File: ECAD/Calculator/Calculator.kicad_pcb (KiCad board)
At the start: 2 copper layers, 156 x 81.5 mm, 30 parts, among them SW1 Switch_Tactile_ESwitch, SW10 Switch_Tactile_ESwitch, SW11 Switch_Tactile_ESwitch, SW12 Switch_Tactile_ESwitch, SW13 Switch_Tactile_ESwitch, SW14 Switch_Tactile_ESwitch, SW15 Switch_Tactile_ESwitch, SW16 Switch_Tactile_ESwitch, SW17 Switch_Tactile_ESwitch, SW18 Switch_Tactile_ESwitch, SW19 Switch_Tactile_ESwitch, SW2 Switch_Tactile_ESwitch, SW20 Switch_Tactile_ESwitch, SW3 Switch_Tactile_ESwitch, SW4 Switch_Tactile_ESwitch, SW5 Switch_Tactile_ESwitch, SW6 Switch_Tactile_ESwitch, SW7 Switch_Tactile_ESwitch, SW8 Switch_Tactile_ESwitch, SW9 Switch_Tactile_ESwitch

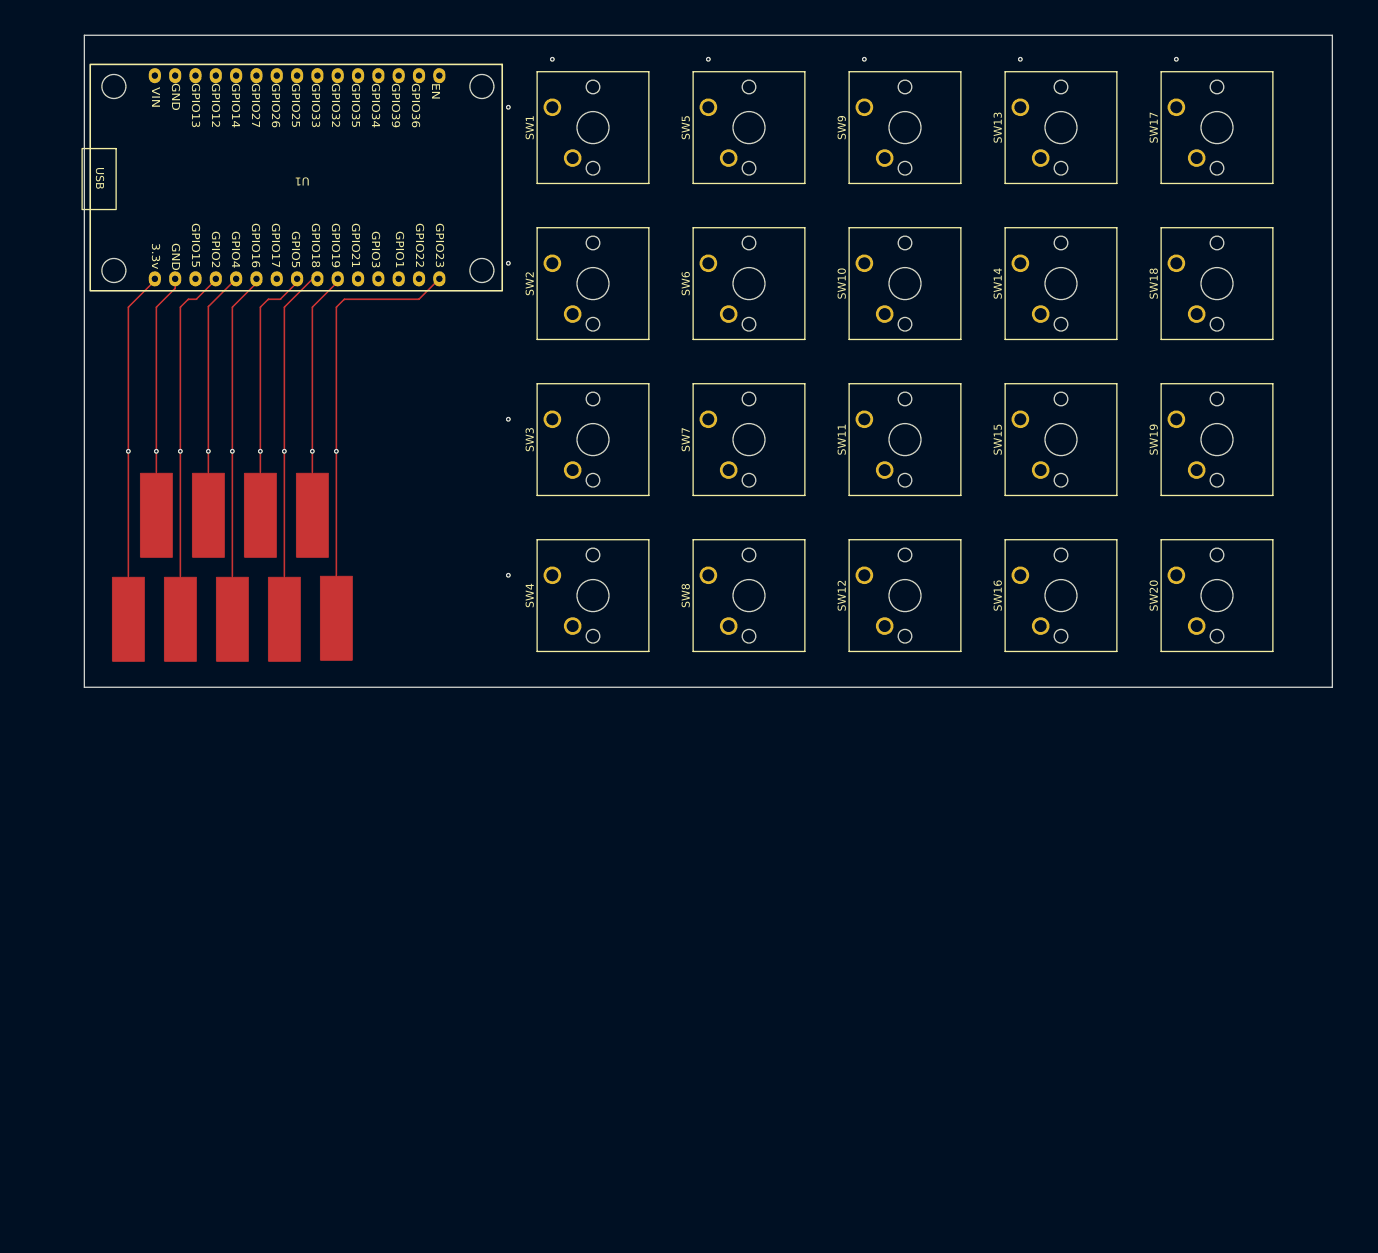
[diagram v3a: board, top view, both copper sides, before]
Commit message: Fixed switch placement
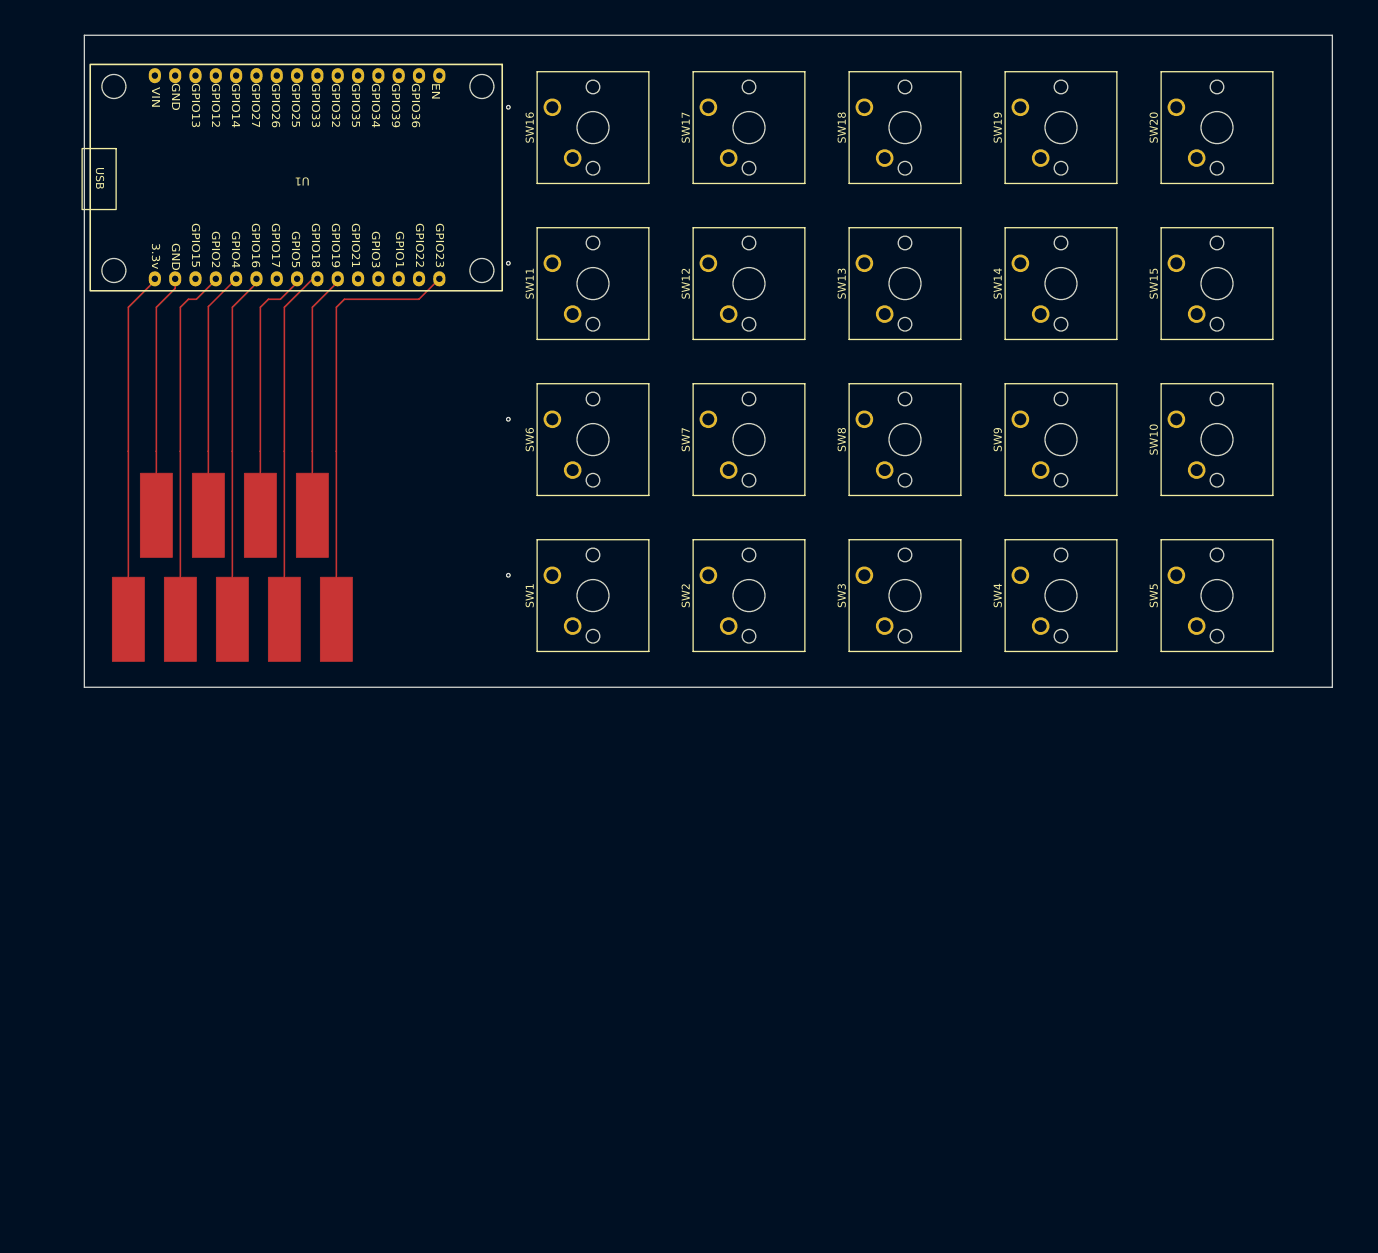
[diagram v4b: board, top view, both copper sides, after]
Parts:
- moved SW16 82.7 mm to (84.5, 27.0)
- moved SW5 82.7 mm to (162.5, 85.5)
- moved SW1 58.5 mm to (84.5, 85.5)
- moved SW17 58.5 mm to (104.0, 27.0)
- moved SW20 58.5 mm to (162.5, 27.0)
- moved SW4 58.5 mm to (143.0, 85.5)
- moved SW10 43.6 mm to (162.5, 66.0)
- moved SW11 43.6 mm to (84.5, 46.5)
- moved SW12 43.6 mm to (104.0, 46.5)
- moved SW18 43.6 mm to (123.5, 27.0)
- moved SW19 43.6 mm to (143.0, 27.0)
- moved SW2 43.6 mm to (104.0, 85.5)
- moved SW3 43.6 mm to (123.5, 85.5)
- moved SW9 43.6 mm to (143.0, 66.0)
- moved SW13 27.6 mm to (123.5, 46.5)
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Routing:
- net /VCC: vias 1 -> 0
- net /SDO(MISO): vias 1 -> 0
- net /SDI(MOSI): vias 1 -> 0
- net /SCK: vias 1 -> 0
- net /RESET: vias 1 -> 0
- net /LED: vias 1 -> 0
- net /GND: vias 1 -> 0
- net /DC/RS: vias 1 -> 0
- net /CS: vias 1 -> 0
- net (no net): vias 9 -> 4

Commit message: Refactor schematic: Remove unnecessary wires and update connections in Calculator.kicad_sch Added keyboard matrix wiring in PCB and mounting holes for enclosure
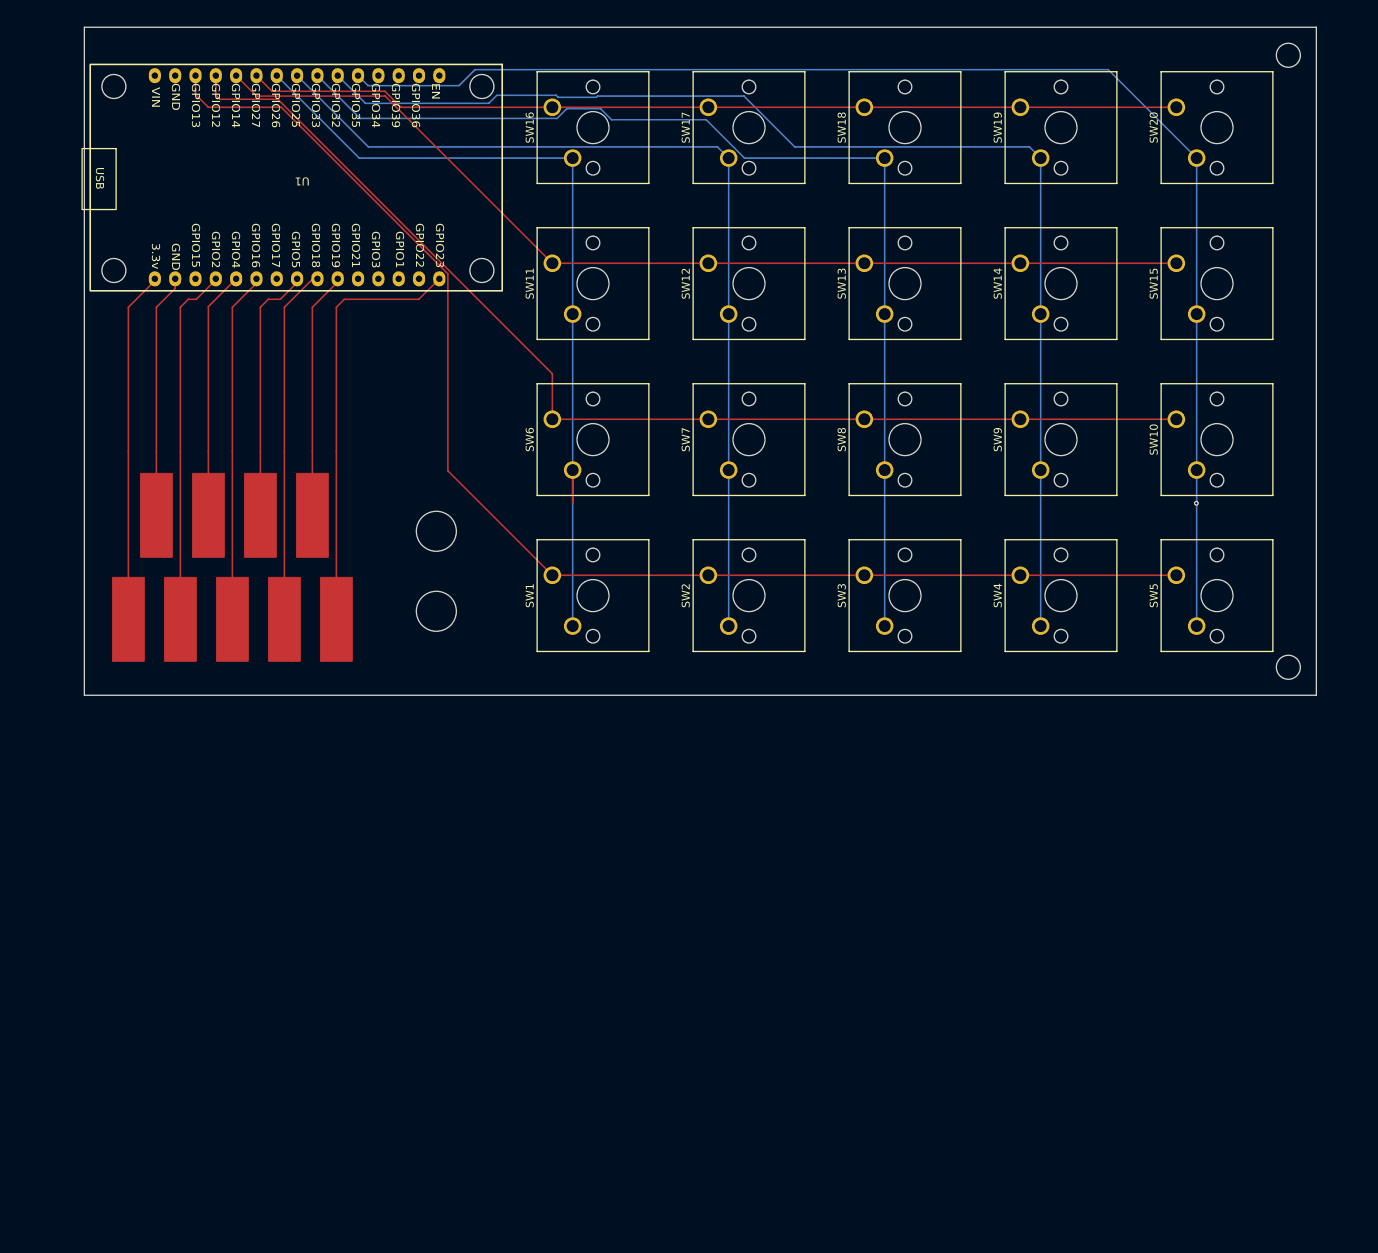
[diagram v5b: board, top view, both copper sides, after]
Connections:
- SW1 pad 2: /Col 1 -> /Row A
- SW10 pad 2: /Col 2 -> /Row E
- SW11 pad 2: /Col 3 -> /Row A
- SW12 pad 2: /Col 3 -> /Row B
- SW13 pad 2: /Col 3 -> /Row C
- SW14 pad 2: /Col 3 -> /Row D
- SW15 pad 2: /Col 3 -> /Row E
- SW16 pad 2: /Col 4 -> /Row A
- SW17 pad 2: /Col 4 -> /Row B
- SW18 pad 2: /Col 4 -> /Row C
- SW19 pad 2: /Col 4 -> /Row D
- SW2 pad 2: /Col 1 -> /Row B
- SW20 pad 2: /Col 4 -> /Row E
- SW3 pad 2: /Col 1 -> /Row C
- SW4 pad 2: /Col 1 -> /Row D
- SW5 pad 2: /Col 1 -> /Row E
- SW6 pad 2: /Col 2 -> /Row A
- SW7 pad 2: /Col 2 -> /Row B
- SW8 pad 2: /Col 2 -> /Row C
- SW9 pad 2: /Col 2 -> /Row D
- U1 pad 3: /Col 4 -> /Col 1
- U1 pad 4: /Col 3 -> /Col 2
- U1 pad 5: /Col 2 -> /Col 3
- U1 pad 6: /Col 1 -> /Col 4
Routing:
- net /Row E: track 0.00 -> 169.2 mm, vias 0 -> 1
- net /Col 1: track 0.00 -> 164.3 mm
- net /Row D: track 0.00 -> 151.6 mm
- net /Col 2: track 0.00 -> 142.6 mm
- net /Row C: track 0.00 -> 134.7 mm
- net /Col 3: track 0.00 -> 127.2 mm
- net /Row B: track 0.00 -> 116.7 mm
- net /Col 4: track 0.00 -> 116.6 mm
- net /Row A: track 0.00 -> 103.9 mm
- net (no net): vias 4 -> 0
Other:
- board size 156 x 81.5 mm -> 154 x 83.5 mm

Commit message: Added silkscreen notations to PCB, as well as logo and designation.
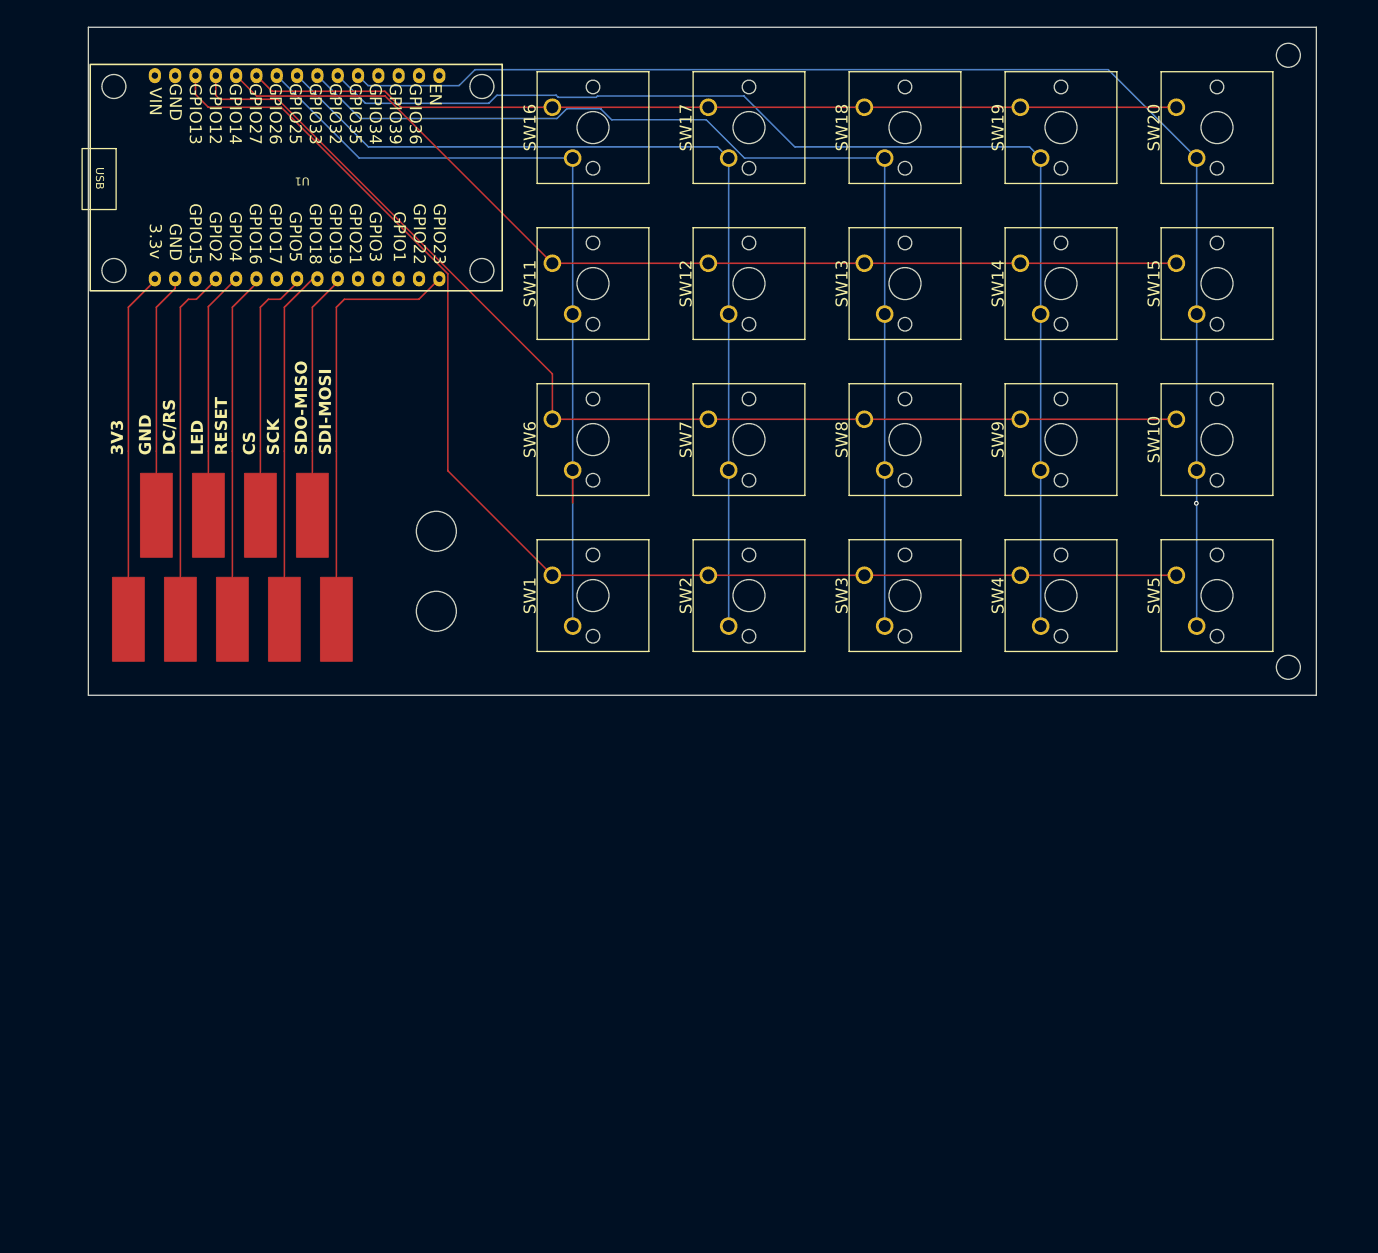
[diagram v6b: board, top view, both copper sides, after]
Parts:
- added G***: LOGO, LOGO, B.Cu at (47.5, 79.0)
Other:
- board size 154 x 83.5 mm -> 153.5 x 83.5 mm
- board text added: "3V3"
- board text added: "CALCULATOR 1"
- board text added: "CS"
- board text added: "DC/RS"
- board text added: "GND"
- board text added: "LED"
- board text added: "RESET"
- board text added: "SCK"
- board text added: "SDI-MOSI"
- board text added: "SDO-MISO"

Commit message: Changed Various GPIO pins to avoid issures with missing pull-up resistors, and flash pins
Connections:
- U1 pad 11: /Row E -> unconnected-(U1-GPIO35-Pad11)
- U1 pad 26: unconnected-(U1-GPIO21-Pad26) -> /Row E
- U1 pad 29: unconnected-(U1-GPIO22-Pad29) -> /Col 2
- U1 pad 4: /Col 2 -> unconnected-(U1-GPIO12-Pad4)
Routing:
- net /Row E: track 169.2 -> 210.3 mm
- net /Col 2: track 142.6 -> 102.5 mm
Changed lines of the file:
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@@
 			(layers "*.Cu" "*.Mask")
 			(remove_unused_layers no)
-			(net "/Col 2")
+			(net "unconnected-(U1-GPIO12-Pad4)")
 			(pinfunction "GPIO12_4")
-			(pintype "bidirectional")
+			(pintype "bidirectional+no_connect")
 		)
 		(pad "5" thru_hole oval
@@
 			(layers "*.Cu" "*.Mask")
 			(remove_unused_layers no)
-			(net "/Row E")
+			(net "unconnected-(U1-GPIO35-Pad11)")
 			(pinfunction "GPIO35_11")
-			(pintype "bidirectional")
+			(pintype "bidirectional+no_connect")
 		)
 		(pad "12" thru_hole oval
@@
 			(layers "*.Cu" "*.Mask")
 			(remove_unused_layers no)
-			(net "unconnected-(U1-GPIO21-Pad26)")
+			(net "/Row E")
 			(pinfunction "GPIO21_26")
-			(pintype "bidirectional+no_connect")
+			(pintype "bidirectional")
 		)
 		(pad "27" thru_hole oval
@@
 			(layers "*.Cu" "*.Mask")
 			(remove_unused_layers no)
-			(net "unconnected-(U1-GPIO22-Pad29)")
+			(net "/Col 2")
 			(pinfunction "GPIO22_29")
-			(pintype "bidirectional+no_connect")
+			(pintype "bidirectional")
 		)
 		(pad "30" thru_hole oval
@@
 	)
 	(segment
-		(start 50.182937 26)
-		(end 42.932277 26)
-		(width 0.2)
-		(layer "F.Cu")
-		(net "/Col 2")
-	)
-	(segment
 		(start 84.5 66)
 		(end 162.5 66)
@@
 	)
 	(segment
-		(start 84.5 66)
-		(end 84.5 60.317063)
+		(start 67.832277 48.44492)
+		(end 67.832277 49.332277)
 		(width 0.2)
-		(layer "F.Cu")
-		(net "/Col 2")
-	)
-	(segment
-		(start 42.932277 26)
-		(end 42.432277 25.5)
-		(width 0.2)
-		(layer "F.Cu")
-		(net "/Col 2")
-	)
-	(segment
-		(start 84.5 60.317063)
-		(end 50.182937 26)
-		(width 0.2)
-		(layer "F.Cu")
+		(layer "B.Cu")
 		(net "/Col 2")
 	)
 	(segment
-		(start 42.432277 25.5)
-		(end 42.432277 23.04492)
+		(start 67.832277 49.332277)
+		(end 84.5 66)
 		(width 0.2)
-		(layer "F.Cu")
+		(layer "B.Cu")
 		(net "/Col 2")
 	)
@@
 	)
 	(segment
-		(start 74.822241 22.30246)
-		(end 72.829781 24.29492)
+		(start 153.48492 21.79492)
+		(end 165.04 33.35)
 		(width 0.2)
 		(layer "B.Cu")
@@
 	)
 	(segment
-		(start 61.462277 24.29492)
-		(end 60.212277 23.04492)
+		(start 48.990277 22.417025)
+		(end 49.612382 21.79492)
 		(width 0.2)
 		(layer "B.Cu")
@@
 	)
 	(segment
-		(start 165.04 33.35)
-		(end 165.04 91.85)
+		(start 48.990277 37.22292)
+		(end 48.990277 22.417025)
 		(width 0.2)
 		(layer "B.Cu")
@@
 	(segment
 		(start 165.04 33.35)
-		(end 153.99246 22.30246)
+		(end 165.04 91.85)
 		(width 0.2)
 		(layer "B.Cu")
@@
 	)
 	(segment
-		(start 72.829781 24.29492)
-		(end 61.462277 24.29492)
+		(start 49.612382 21.79492)
+		(end 153.48492 21.79492)
 		(width 0.2)
 		(layer "B.Cu")
@@
 	)
 	(segment
-		(start 153.99246 22.30246)
-		(end 74.822241 22.30246)
+		(start 60.212277 48.44492)
+		(end 48.990277 37.22292)
 		(width 0.2)
 		(layer "B.Cu")
